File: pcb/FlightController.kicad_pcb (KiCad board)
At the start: 4 copper layers, 36 x 36 mm, 63 parts, among them P1 3V3, P10 SWDIO, P11 SWCLK, P2 USB_OTG, P3 CONN_02X04, P4 CKD_SANDWICH, P5 CONN_02X10, P6 RESET, P7 BOOT0, P8 CONN_01X01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

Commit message: Final gerbers for test manufacturing run.
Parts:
- P2: footprint fci:Mini-USB-B -> fci:Mini-USB-B-EDGE
- moved P2 1.20 mm to (142.3, 92.7)
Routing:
- net GNDPWR: track 143.7 -> 152.1 mm
- net (no net): track 0.00 -> 0.67 mm
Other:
- outline, holes or cut-outs redrawn
- board text added: "F3FC v8"
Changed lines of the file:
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@@
 (kicad_pcb (version 4) (host pcbnew 4.0.1-stable)
   (general
-    (links 200)
+    (links 202)
     (no_connects 0)
-    (area 129.924999 89.924999 166.075001 126.075001)
+    (area 111.750001 73.15 183.535715 196.5)
     (thickness 1.6)
-    (drawings 68)
-    (tracks 1622)
+    (drawings 77)
+    (tracks 1625)
     (zones 0)
     (modules 63)
@@
     (39 F.Mask user)
     (40 Dwgs.User user)
-    (41 Cmts.User user hide)
+    (41 Cmts.User user)
     (42 Eco1.User user hide)
     (43 Eco2.User user hide)
@@
     (47 F.CrtYd user)
     (48 B.Fab user)
-    (49 F.Fab user)
+    (49 F.Fab user hide)
   )
   (setup
@@
       (xy 0.041912 -1.810672)) (layer F.Cu) (width 0.01))
   )
-  (module fci:Mini-USB-B (layer B.Cu)
-    (at 142.3 91.45)
-    (fp_text reference P2 (at -6.78 1.46) (layer B.SilkS) hide
-      (effects (font (size 1 1) (thickness 0.15)) (justify mirror))
-    )
-    (fp_text value USB_OTG (at -0.02 4.63) (layer B.Fab)
-      (effects (font (size 1 1) (thickness 0.15)) (justify mirror))
-    )
-    (fp_line (start -3.45 -1.45) (end 3.45 -1.45) (layer B.Fab) (width 0.15))
-    (pad 6 smd rect (at -3.2 2.45) (size 1.6 1.4) (layers B.Cu B.Paste B.Mask)
-      (net 2 GNDPWR))
-    (pad 6 smd rect (at 3.2 2.45) (size 1.6 1.4) (layers B.Cu B.Paste B.Mask)
-      (net 2 GNDPWR))
-    (pad 1 smd rect (at -1.3 2.675) (size 0.4 1.35) (layers B.Cu B.Paste B.Mask)
-      (net 7 +5VA))
-    (pad 2 smd rect (at -0.65 2.675) (size 0.4 1.35) (layers B.Cu B.Paste B.Mask)
-      (net 132 /USB_D-))
-    (pad 3 smd rect (at 0 2.675) (size 0.4 1.35) (layers B.Cu B.Paste B.Mask)
-      (net 133 /USB_D+))
-    (pad 4 smd rect (at 0.65 2.675) (size 0.4 1.35) (layers B.Cu B.Paste B.Mask)
-      (net 9 "Net-(P2-Pad4)"))
-    (pad 5 smd rect (at 1.3 2.675) (size 0.4 1.35) (layers B.Cu B.Paste B.Mask)
-      (net 2 GNDPWR))
-    (pad 6 smd rect (at -1.2 0) (size 1.9 1.9) (layers B.Cu B.Paste B.Mask)
-      (net 2 GNDPWR))
-    (pad 6 smd rect (at 1.2 0) (size 1.9 1.9) (layers B.Cu B.Paste B.Mask)
-      (net 2 GNDPWR))
-    (pad 6 thru_hole oval (at -3.3 0) (size 0.9 1.6) (drill oval 0.5 1.2) (layers *.Cu *.Mask B.SilkS)
-      (net 2 GNDPWR))
-    (pad 6 thru_hole oval (at 3.3 0) (size 0.9 1.6) (drill oval 0.5 1.2) (layers *.Cu *.Mask B.SilkS)
-      (net 2 GNDPWR))
-  )
   (module polystack:polystack-medium-10mm (layer F.Cu)
     (at 160.85 120.45)
@@
       (xy 3.654557 0.555617)) (layer F.SilkS) (width 0))
   )
+  (module fci:Mini-USB-B-EDGE (layer B.Cu)
+    (at 142.3 92.65)
+    (fp_text reference P2 (at -6.78 1.46) (layer B.SilkS) hide
+      (effects (font (size 1 1) (thickness 0.15)) (justify mirror))
+    )
+    (fp_text value USB_OTG (at -0.02 3.43) (layer B.Fab)
+      (effects (font (size 1 1) (thickness 0.15)) (justify mirror))
+    )
+    (fp_arc (start -3.3 -1.55) (end -3.05 -1.55) (angle -180) (layer B.Fab) (width 0.15))
+    (fp_line (start -3.05 -0.85) (end -3.05 -1.55) (layer B.Fab) (width 0.15))
+    (fp_line (start -3.55 -0.85) (end -3.55 -1.55) (layer B.Fab) (width 0.15))
+    (fp_line (start -3.45 -2.65) (end 3.45 -2.65) (layer B.Fab) (width 0.15))
+    (fp_arc (start -3.3 -0.85) (end -3.55 -0.85) (angle -180) (layer B.Fab) (width 0.15))
+    (fp_arc (start 3.3 -0.85) (end 3.05 -0.85) (angle -180) (layer B.Fab) (width 0.15))
+    (fp_line (start 3.05 -0.85) (end 3.05 -1.55) (layer B.Fab) (width 0.15))
+    (fp_line (start 3.55 -0.85) (end 3.55 -1.55) (layer B.Fab) (width 0.15))
+    (fp_arc (start 3.3 -1.55) (end 3.55 -1.55) (angle -180) (layer B.Fab) (width 0.15))
+    (pad 6 smd rect (at -3.2 1.25) (size 1.6 1.4) (layers B.Cu B.Paste B.Mask)
+      (net 2 GNDPWR))
+    (pad 6 smd rect (at 3.2 1.25) (size 1.6 1.4) (layers B.Cu B.Paste B.Mask)
+      (net 2 GNDPWR))
+    (pad 1 smd rect (at -1.3 1.475) (size 0.4 1.35) (layers B.Cu B.Paste B.Mask)
+      (net 7 +5VA))
+    (pad 2 smd rect (at -0.65 1.475) (size 0.4 1.35) (layers B.Cu B.Paste B.Mask)
+      (net 132 /USB_D-))
+    (pad 3 smd rect (at 0 1.475) (size 0.4 1.35) (layers B.Cu B.Paste B.Mask)
+      (net 133 /USB_D+))
+    (pad 4 smd rect (at 0.65 1.475) (size 0.4 1.35) (layers B.Cu B.Paste B.Mask)
+      (net 9 "Net-(P2-Pad4)"))
+    (pad 5 smd rect (at 1.3 1.475) (size 0.4 1.35) (layers B.Cu B.Paste B.Mask)
+      (net 2 GNDPWR))
+    (pad 6 smd rect (at -1.2 -1.2) (size 1.9 1.9) (layers B.Cu B.Paste B.Mask)
+      (net 2 GNDPWR))
+    (pad 6 smd rect (at 1.2 -1.2) (size 1.9 1.9) (layers B.Cu B.Paste B.Mask)
+      (net 2 GNDPWR))
+    (pad 6 smd oval (at -3.3 -1.2) (size 0.9 1.6) (layers B.Cu B.Paste B.Mask)
+      (net 2 GNDPWR))
+    (pad 6 smd oval (at 3.3 -1.2) (size 0.9 1.6) (layers B.Cu B.Paste B.Mask)
+      (net 2 GNDPWR))
+    (pad 6 smd oval (at -3.3 -1.2) (size 0.9 1.6) (layers F.Cu F.Mask)
+      (net 2 GNDPWR))
+    (pad 6 smd oval (at 3.3 -1.2) (size 0.9 1.6) (layers F.Cu F.Mask)
+      (net 2 GNDPWR))
+  )
+  (gr_arc (start 145.6 91.8) (end 145.85 91.8) (angle 180) (layer Edge.Cuts) (width 0.15))
+  (gr_line (start 145.85 91.1) (end 145.85 91.8) (layer Edge.Cuts) (width 0.15))
+  (gr_line (start 145.35 91.1) (end 145.35 91.8) (layer Edge.Cuts) (width 0.15))
+  (gr_arc (start 145.6 91.1) (end 145.35 91.1) (angle 180) (layer Edge.Cuts) (width 0.15))
+  (gr_arc (start 139 91.8) (end 139.25 91.8) (angle 180) (layer Edge.Cuts) (width 0.15))
+  (gr_arc (start 139 91.1) (end 138.75 91.1) (angle 180) (layer Edge.Cuts) (width 0.15))
+  (gr_line (start 139.25 91.1) (end 139.25 91.8) (layer Edge.Cuts) (width 0.15))
+  (gr_line (start 138.75 91.1) (end 138.75 91.8) (layer Edge.Cuts) (width 0.15))
+  (gr_text "F3FC v8" (at 173.4 195.3) (layer Cmts.User)
+    (effects (font (size 1.5 1.5) (thickness 0.3)))
+  )
   (gr_line (start 152 108.5) (end 151.5 108) (layer F.SilkS) (width 0.6))
   (gr_line (start 153 109.5) (end 152 107.5) (layer F.SilkS) (width 0.6))
@@
   (gr_line (start 166 92.75) (end 166 123.25) (angle 90) (layer Edge.Cuts) (width 0.15))
   (gr_line (start 132.75 90) (end 163.25 90) (angle 90) (layer Edge.Cuts) (width 0.15))
+  (segment (start 145.6 91.45) (end 144.9976 91.45) (width 0.1524) (layer In1.Cu) (net 0))
+  (segment (start 144.9976 91.45) (end 144.9476 91.4) (width 0.1524) (layer In1.Cu) (net 0))
   (via (at 155.699238 105.661094) (size 0.685801) (drill 0.330201) (layers F.Cu B.Cu) (net 1))
   (segment (start 155 105.3) (end 155.338144 105.3) (width 0.1524) (layer In2.Cu) (net 1))
@@
   (segment (start 133.6 116.3424) (end 133.6 116.05) (width 0.1524) (layer F.Cu) (net 1))
   (segment (start 158.11 106.2238) (end 158.072517 106.186317) (width 0.1524) (layer F.Cu) (net 1))
+  (segment (start 139 91.45) (end 139 93.8) (width 0.1524) (layer B.Cu) (net 2))
+  (segment (start 139 93.8) (end 139.1 93.9) (width 0.1524) (layer B.Cu) (net 2))
+  (segment (start 146.15 92.7) (end 146.15 92) (width 0.1524) (layer F.Cu) (net 2))
+  (segment (start 146.15 92) (end 145.6 91.45) (width 0.1524) (layer F.Cu) (net 2))
+  (segment (start 145.6 91.45) (end 139 91.45) (width 0.1524) (layer F.Cu) (net 2))
+  (segment (start 145.6 91.45) (end 143.5 91.45) (width 0.1524) (layer B.Cu) (net 2))
   (segment (start 157 105) (end 156.629798 105) (width 0.1524) (layer F.Cu) (net 2))
   (segment (start 155.657101 104.657101) (end 155.900452 104.900452) (width 0.1524) (layer In1.Cu) (net 2))
@@
   (segment (start 147.03755 124.9) (end 146.216 124.9) (width 0.1524) (layer B.Cu) (net 2))
   (segment (start 146.216 124.9) (end 145.2 124.9) (width 0.1524) (layer B.Cu) (net 2))
-  (segment (start 143.5 91.45) (end 145.6 91.45) (width 0.1524) (layer B.Cu) (net 2))
   (segment (start 141.1 91.45) (end 142.2024 91.45) (width 0.1524) (layer B.Cu) (net 2))
   (segment (start 142.2024 91.45) (end 143.5 91.45) (width 0.1524) (layer B.Cu) (net 2))
   (segment (start 139 91.45) (end 141.1 91.45) (width 0.1524) (layer B.Cu) (net 2))
-  (segment (start 146.15 92.7) (end 146.15 92) (width 0.1524) (layer In1.Cu) (net 2))
-  (segment (start 146.15 92) (end 145.6 91.45) (width 0.1524) (layer In1.Cu) (net 2))
   (segment (start 145.5 93.0476) (end 145.8476 92.7) (width 0.1524) (layer B.Cu) (net 2))
   (segment (start 145.8476 92.7) (end 146.15 92.7) (width 0.1524) (layer B.Cu) (net 2))
   (segment (start 145.5 93.9) (end 145.5 93.0476) (width 0.1524) (layer B.Cu) (net 2))
   (via (at 146.15 92.7) (size 0.6858) (drill 0.3302) (layers F.Cu B.Cu) (net 2))
-  (segment (start 145.6 91.45) (end 144.9976 91.45) (width 0.1524) (layer In1.Cu) (net 2))
-  (segment (start 144.9976 91.45) (end 144.9476 91.4) (width 0.1524) (layer In1.Cu) (net 2))
   (segment (start 155.07 94.54) (end 155.07 96.17) (width 0.254) (layer F.Cu) (net 2))
   (segment (start 155.07 96.17) (end 155.8 96.9) (width 0.254) (layer F.Cu) (net 2))

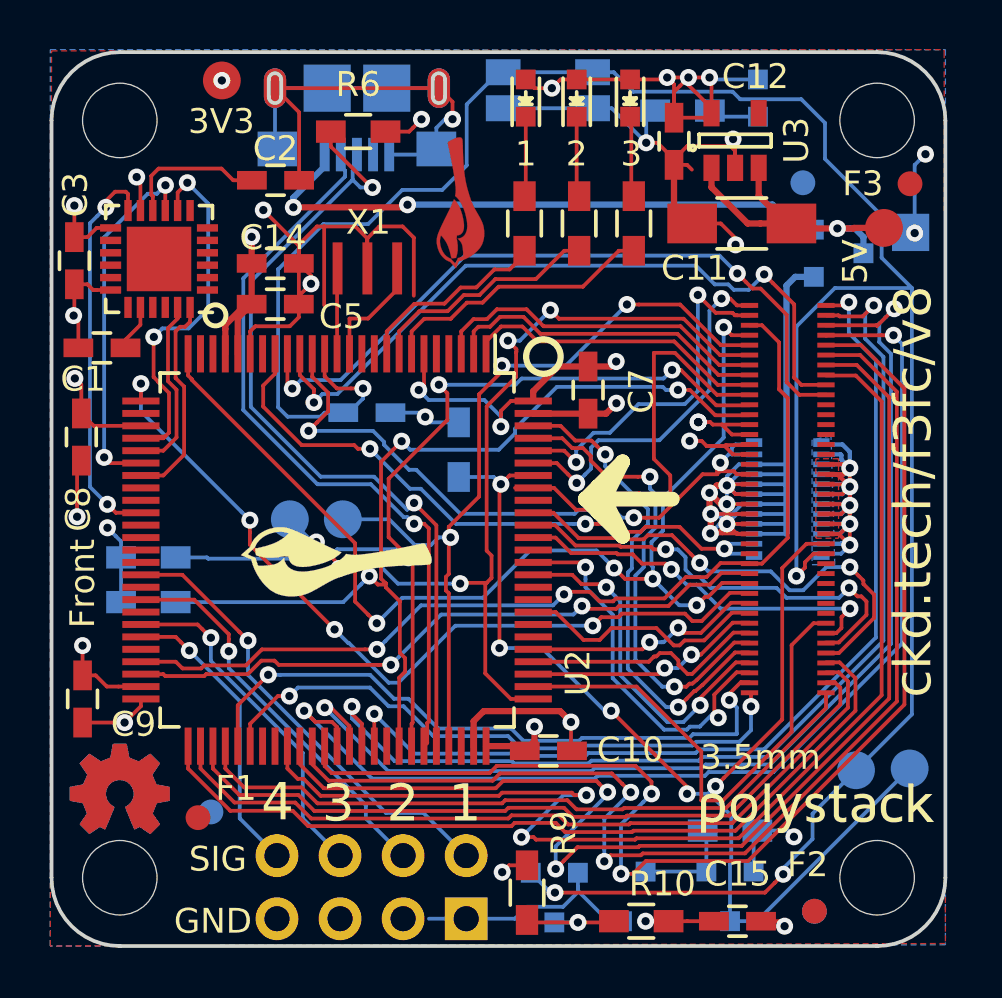
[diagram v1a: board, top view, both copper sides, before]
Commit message: Update polystack logo to bold variant and bump version number.
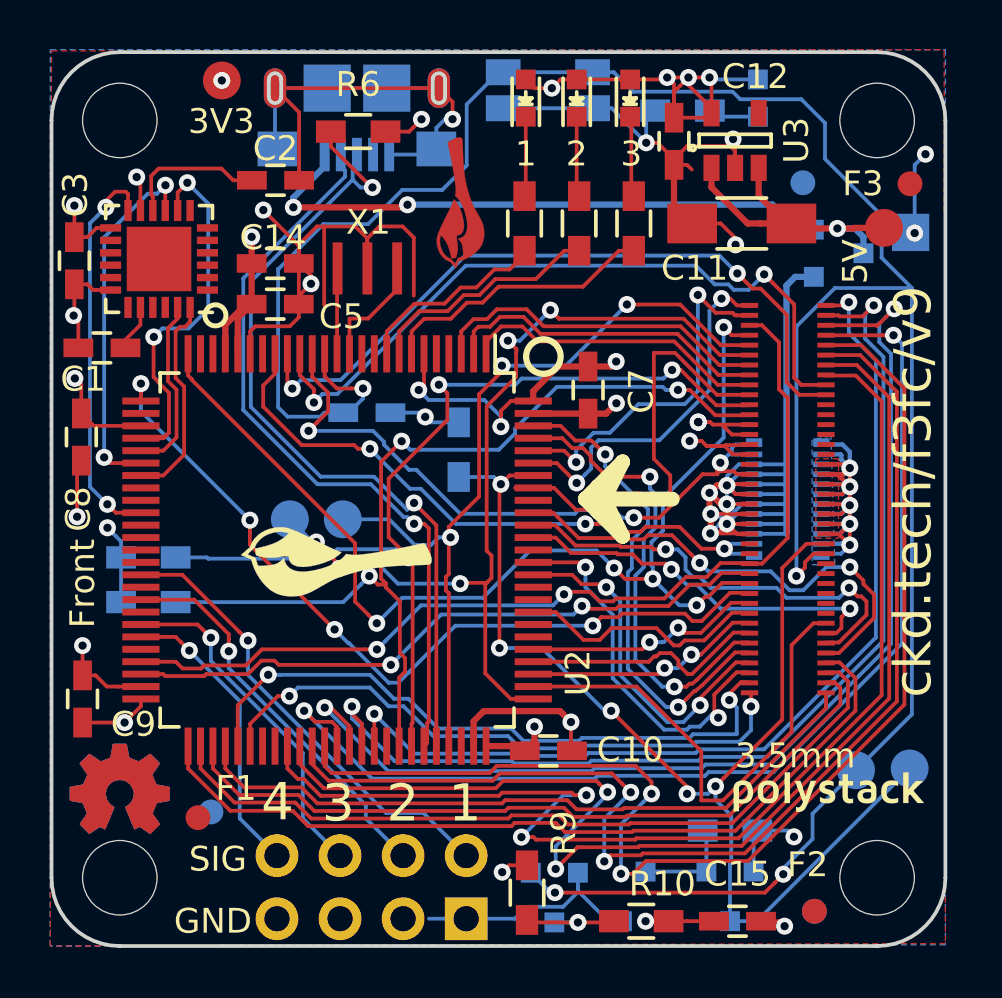
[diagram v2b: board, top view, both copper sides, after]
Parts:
- removed the svg2mod at (160.8, 120.5)
- added svg2mod: G***, polystack:polystack-bold-0.4, F.Cu at (161.3, 119.8)
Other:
- board text added: "ckd.tech/f3fc/v9"
- board text removed: "ckd.tech/f3fc/v8"

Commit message: Add license information to many files. PCB design files are CC-BY and code is MIT license.
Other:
- board text added: "Copyright 2016 Chickadee Tech LLC, <add attributions here> This work is licensed under the Creative Commons Attribution 4.0 International License. To view a copy of this license, visit http://creativecommons.org/licenses/by/4.0/ or send a letter to Creative Commons, PO Box 1866, Mountain View, CA 94042, USA."
- board text added: "Remove all Chickadee Tech LLC trademarks before making your own board. The Chickadee logo and Polystack logo are owned by Chickadee Tech LLC. You may license the Polystack logo for free by emailing support@chickadee.tech and receiving express written permission from Chickadee Tech LLC."
- board text added: "The gear logo is a mark designating open source hardware. Remove it if your design does not comply with the open source hardware definition."
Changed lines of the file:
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@@
     (area 111.750001 73.15 183.535715 196.5)
     (thickness 1.6)
-    (drawings 78)
+    (drawings 85)
     (tracks 1625)
     (zones 0)
@@
     (40 Dwgs.User user)
     (41 Cmts.User user)
-    (42 Eco1.User user hide)
-    (43 Eco2.User user hide)
+    (42 Eco1.User user)
+    (43 Eco2.User user)
     (44 Edge.Cuts user)
     (45 Margin user)
@@
       (xy 2.990233 0.444493)) (layer F.SilkS) (width 0))
   )
+  (gr_line (start 145.37 96.87) (end 106.4 99.04) (layer Cmts.User) (width 0.4))
+  (gr_line (start 106.4 99.04) (end 136.98 109.89) (layer Cmts.User) (width 0.4))
+  (gr_line (start 157.21 119.95) (end 106.4 99.04) (layer Cmts.User) (width 0.4))
+  (gr_text "Remove all Chickadee Tech LLC trademarks\nbefore making your own board. The\nChickadee logo and Polystack logo\nare owned by Chickadee Tech LLC.\n\nYou may license the Polystack logo for\nfree by emailing support@chickadee.tech\nand receiving express written permission\nfrom Chickadee Tech LLC." (at 65.71 100.69) (layer Cmts.User)
+    (effects (font (size 1.5 1.5) (thickness 0.3)) (justify left))
+  )
+  (gr_line (start 131.07 121.67) (end 102.42 128.35) (layer Cmts.User) (width 0.4))
+  (gr_text "The gear logo is a mark designating open\nsource hardware. Remove it if your design\ndoes not comply with the open source\nhardware definition." (at 80.44 133.44) (layer Cmts.User)
+    (effects (font (size 1.5 1.5) (thickness 0.3)) (justify left))
+  )
+  (gr_text "Copyright 2016 Chickadee Tech LLC, <add attributions here>\n\nThis work is licensed under the Creative Commons Attribution 4.0 International License.\nTo view a copy of this license, visit http://creativecommons.org/licenses/by/4.0/\nor send a letter to Creative Commons, PO Box 1866, Mountain View, CA 94042, USA." (at 161.3 179.61) (layer Cmts.User)
+    (effects (font (size 1.5 1.5) (thickness 0.3)) (justify left))
+  )
   (gr_circle (center 157.35 105) (end 157.55 105) (layer B.SilkS) (width 0.4))
